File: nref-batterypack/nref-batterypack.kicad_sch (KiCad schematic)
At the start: 65 parts, among them J1 BACK_CONN, J2 C4+, J3 C3-, J4 C2+, J5 C1-, J6 C1-, J7 PACK_CONN, Q1 BC817, Q2 BC817, Q3 BC817, Q4 BC817, Q5 AO3401A, Q6 DMT2005UDV, Q7 AO3401A, SW1 Reset, U1 BQ76922

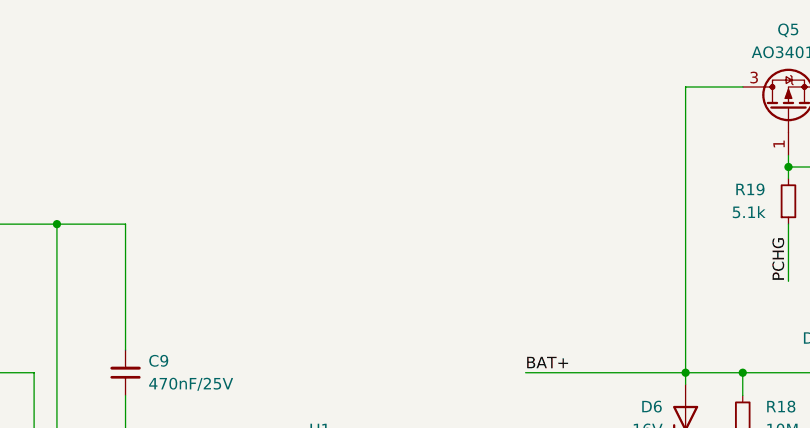
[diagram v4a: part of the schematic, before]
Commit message: batterypack front/back: update board outline/mounting holes
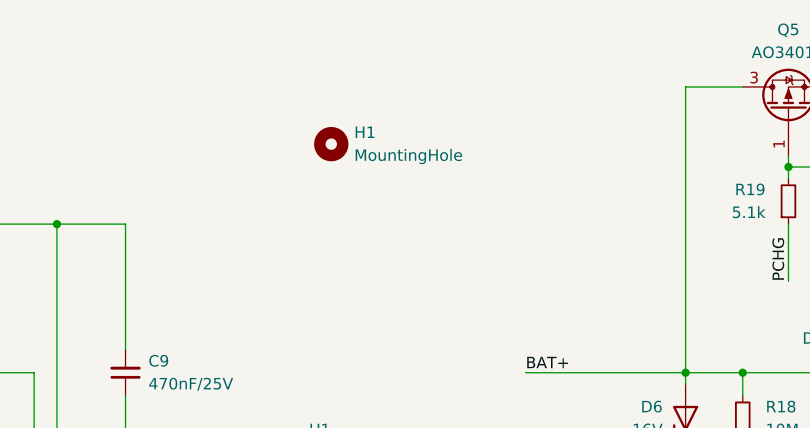
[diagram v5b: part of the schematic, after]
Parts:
- added H1: MountingHole, MountingHole:MountingHole_2.2mm_M2, symbol Mechanical:MountingHole
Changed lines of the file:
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@@
+	)
+	(symbol
+		(lib_id "Mechanical:MountingHole")
+		(at 151.13 38.1 0)
+		(unit 1)
+		(exclude_from_sim yes)
+		(in_bom no)
+		(on_board yes)
+		(dnp no)
+		(fields_autoplaced yes)
+		(property "Reference" "H1"
+			(at 153.67 36.8299 0)
+			(effects
+				(font
+					(size 1.27 1.27)
+				)
+				(justify left)
+			)
+		)
+		(property "Value" "MountingHole"
+			(at 153.67 39.3699 0)
+			(effects
+				(font
+					(size 1.27 1.27)
+				)
+				(justify left)
+			)
+		)
+		(property "Footprint" "MountingHole:MountingHole_2.2mm_M2"
+			(at 151.13 38.1 0)
+			(effects
+				(font
+					(size 1.27 1.27)
+				)
+				(hide yes)
+			)
+		)
+		(property "Datasheet" "~"
+			(at 151.13 38.1 0)
+			(effects
+				(font
+					(size 1.27 1.27)
+				)
+				(hide yes)
+			)
+		)
+		(property "Description" "Mounting Hole without connection"
+			(at 151.13 38.1 0)
+			(effects
+				(font
+					(size 1.27 1.27)
+				)
+				(hide yes)
+			)
+		)
+		(instances
+			(project ""
+				(path "/49c88381-2fae-4c42-af1a-831661a524e4"
+					(reference "H1")
+					(unit 1)
+				)
+			)
+		)
 	)
 	(symbol

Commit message: add latest PCB updates
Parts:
- H1: MPN (none) -> DNP; Manufacturer (none) -> DNP; now not fitted
- J1: footprint Connector_JST:JST_SHL_SM02B-SHLS-TF_1x02-1MP_P1.00mm_Horizontal -> Connector_JST:JST_SH_SM02B-SRSS-TB_1x02-1MP_P1.00mm_Horizontal
- J2, J3, J4, J5: MPN S7131-45R -> S1741-46R
- J7: footprint Connector_JST:JST_SHL_SM07B-SHLS-TF_1x07-1MP_P1.00mm_Horizontal -> Connector_JST:JST_SH_SM07B-SRSS-TB_1x07-1MP_P1.00mm_Horizontal
- R26: MPN RC0402JR-071KL -> (none)
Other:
- note added: "TODO: this was the wrong part, SHL instead of SH! TODO: fix footprint in layout"
- note added: "TODO: was wrong footprint!"
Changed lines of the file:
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@@
 		)
 	)
+	(text "TODO: this was the wrong part, SHL instead of SH!\nTODO: fix footprint in layout"
+		(exclude_from_sim no)
+		(at 2.794 95.758 0)
+		(effects
+			(font
+				(size 1.27 1.27)
+			)
+		)
+	)
+	(text "TODO: this was the wrong part, SHL instead of SH!\nTODO: fix footprint in layout"
+		(exclude_from_sim no)
+		(at 236.982 115.57 0)
+		(effects
+			(font
+				(size 1.27 1.27)
+			)
+		)
+	)
+	(text "TODO: was wrong footprint!"
+		(exclude_from_sim no)
+		(at 239.268 24.13 0)
+		(effects
+			(font
+				(size 1.27 1.27)
+			)
+		)
+	)
 	(label "DSG"
 		(at 168.91 113.03 180)
@@
 			)
 		)
-		(property "MPN" "RC0402JR-071KL"
+		(property "MPN" ""
 			(at 238.76 31.75 0)
 			(effects
@@
 			)
 		)
-		(property "MPN" "S7131-45R"
+		(property "MPN" "S1741-46R"
 			(at 36.83 106.68 0)
 			(effects
@@
 			)
 		)
-		(property "Footprint" "Connector_JST:JST_SHL_SM02B-SHLS-TF_1x02-1MP_P1.00mm_Horizontal"
+		(property "Footprint" "Connector_JST:JST_SH_SM02B-SRSS-TB_1x02-1MP_P1.00mm_Horizontal"
 			(at 22.86 107.95 0)
 			(effects
@@
 			)
 		)
-		(property "MPN" "S7131-45R"
+		(property "MPN" "S1741-46R"
 			(at 36.83 146.05 0)
 			(effects
@@
 			)
 		)
-		(property "MPN" "S7131-45R"
+		(property "MPN" "S1741-46R"
 			(at 36.83 63.5 0)
 			(effects
@@
 			)
 		)
-		(property "Footprint" "Connector_JST:JST_SHL_SM07B-SHLS-TF_1x07-1MP_P1.00mm_Horizontal"
+		(property "Footprint" "Connector_JST:JST_SH_SM07B-SRSS-TB_1x07-1MP_P1.00mm_Horizontal"
 			(at 238.76 129.54 0)
 			(effects
@@
 			)
 		)
-		(property "MPN" "S7131-45R"
+		(property "MPN" "S1741-46R"
 			(at 36.83 95.25 0)
 			(effects
@@
 		(in_bom no)
 		(on_board yes)
-		(dnp no)
+		(dnp yes)
 		(fields_autoplaced yes)
 		(property "Reference" "H1"
@@
 			(at 151.13 38.1 0)
 			(effects
+				(font
+					(size 1.27 1.27)
+				)
+				(hide yes)
+			)
+		)
+		(property "MPN" "DNP"
+			(at 151.13 38.1 0)
+			(effects
+				(font
+					(size 1.27 1.27)
+				)
+				(hide yes)
+			)
+		)
+		(property "Manufacturer" "DNP"
+			(at 151.13 38.1 0)
+			(effects

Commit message: batterypack: snapshot before merge
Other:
- note added: "TODO: "however, adding a Zener diode and series resistor on each pin provides more robust ESD performance""
- note added: "TODO: needs ground attachment and/or i2c protection"
- note added: "TODO: what's the return path for i2c and alert?"
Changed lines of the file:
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@@
 (kicad_sch
-	(version 20231120)
+	(version 20250114)
 	(generator "eeschema")
-	(generator_version "8.0")
+	(generator_version "9.0")
 	(paper "A4")
+	(text "TODO: what's the return path for i2c and alert?"
+		(exclude_from_sim no)
+		(at 151.13 147.32 0)
+		(effects
+			(font
+				(size 1.27 1.27)
+			)
+		)
+	)
+	(text "TODO: this was the wrong part, SHL instead of SH!\nTODO: fix footprint in layout"
+		(exclude_from_sim no)
+		(at 2.794 95.758 0)
+		(effects
+			(font
+				(size 1.27 1.27)
+			)
+		)
+	)
+	(text "TODO: \"however, adding a Zener diode and\nseries resistor on each pin provides more robust ESD performance\""
+		(exclude_from_sim no)
+		(at 238.76 104.14 0)
+		(effects
+			(font
+				(size 1.27 1.27)
+			)
+		)
+	)
+	(text "TODO: needs ground attachment and/or i2c protection"
+		(exclude_from_sim no)
+		(at 207.01 144.78 0)
+		(effects
+			(font
+				(size 1.27 1.27)
+			)
+		)
+	)
+	(text "TODO: this was the wrong part, SHL instead of SH!\nTODO: fix footprint in layout"
+		(exclude_from_sim no)
+		(at 236.982 115.57 0)
+		(effects
+			(font
+				(size 1.27 1.27)
+			)
+		)
+	)
+	(text "TODO: was wrong footprint!"
+		(exclude_from_sim no)
+		(at 239.268 24.13 0)
+		(effects
+			(font
+				(size 1.27 1.27)
+			)
+		)
+	)
 	(junction
 		(at 69.85 121.92)
@@
 		)
 	)
-	(text "TODO: this was the wrong part, SHL instead of SH!\nTODO: fix footprint in layout"
-		(exclude_from_sim no)
-		(at 2.794 95.758 0)
-		(effects
-			(font
-				(size 1.27 1.27)
-			)
-		)
-	)
-	(text "TODO: this was the wrong part, SHL instead of SH!\nTODO: fix footprint in layout"
-		(exclude_from_sim no)
-		(at 236.982 115.57 0)
-		(effects
-			(font
-				(size 1.27 1.27)
-			)
-		)
-	)
-	(text "TODO: was wrong footprint!"
-		(exclude_from_sim no)
-		(at 239.268 24.13 0)
-		(effects
-			(font
-				(size 1.27 1.27)
-			)
-		)
-	)
 	(label "DSG"
 		(at 168.91 113.03 180)
-		(fields_autoplaced yes)
 		(effects
 			(font
@@
 	(label "SDA"
 		(at 226.06 129.54 0)
-		(fields_autoplaced yes)
 		(effects
 			(font
@@
 	(label "PACK-"
 		(at 226.06 121.92 0)
-		(fields_autoplaced yes)
 		(effects
 			(font
@@
 	(label "SRP"
 		(at 101.6 163.83 180)
-		(fields_autoplaced yes)
 		(effects
 			(font
@@
 	(label "LD"
 		(at 251.46 82.55 0)
-		(fields_autoplaced yes)
 		(effects
 			(font
@@
 	(label "CHG"
 		(at 209.55 86.36 90)
-		(fields_autoplaced yes)
 		(effects
 			(font
@@
 	(label "ALERT"
 		(at 226.06 127 0)
-		(fields_autoplaced yes)
 		(effects
 			(font
@@
 	(label "VC2"
 		(at 101.6 106.68 180)
-		(fields_autoplaced yes)
 		(effects
 			(font
@@
 	(label "PACK-"
 		(at 226.06 137.16 0)
-		(fields_autoplaced yes)
 		(effects
 			(font
@@
 	(label "PDSG"
 		(at 168.91 107.95 180)
-		(fields_autoplaced yes)
 		(effects
 			(font
@@
 	(label "SCL"
 		(at 226.06 132.08 0)
-		(fields_autoplaced yes)
 		(effects
 			(font
@@
 	(label "PACK-"
 		(at 91.44 179.07 180)
-		(fields_autoplaced yes)
 		(effects
 			(font
@@
 	(label "BAT+"
 		(at 172.72 63.5 0)
-		(fields_autoplaced yes)
 		(effects
 			(font
@@
 	(label "LD"
 		(at 170.18 77.47 180)
-		(fields_autoplaced yes)
 		(effects
 			(font
@@
 	(label "DSG"
 		(at 224.79 86.36 90)
-		(fields_autoplaced yes)
 		(effects
 			(font
@@
 	(label "~{RST}"
 		(at 186.69 100.33 180)
-		(fields_autoplaced yes)
 		(effects
 			(font
@@
 	(label "CHG"
 		(at 168.91 115.57 180)
-		(fields_autoplaced yes)
 		(effects
 			(font
@@
 	(label "SCL"
 		(at 168.91 85.09 180)
-		(fields_autoplaced yes)
 		(effects
 			(font
@@
 	(label "VC4"
 		(at 101.6 83.82 180)
-		(fields_autoplaced yes)
 		(effects
 			(font
@@
 	(label "VC1"
 		(at 101.6 129.54 180)
-		(fields_autoplaced yes)
 		(effects
 			(font
@@
 	(label "PACK+"
 		(at 276.86 63.5 180)
-		(fields_autoplaced yes)
 		(effects
 			(font
@@
 	(label "VC5"
 		(at 101.6 63.5 180)
-		(fields_autoplaced yes)
 		(effects
 			(font
@@
 	(label "PACK"
 		(at 251.46 85.09 0)
-		(fields_autoplaced yes)
 		(effects
 			(font
@@
 	(label "VC0"
 		(at 101.6 151.13 180)
-		(fields_autoplaced yes)
 		(effects
 			(font
@@
 	(label "PCHG"
 		(at 168.91 110.49 180)
-		(fields_autoplaced yes)
 		(effects
 			(font
@@
 	(label "ALERT"
 		(at 168.91 90.17 180)
-		(fields_autoplaced yes)
 		(effects
 			(font
@@
 	(label "PDSG"
 		(at 228.6 53.34 90)
-		(fields_autoplaced yes)
 		(effects
 			(font
@@
 	(label "BAT-"
 		(at 43.18 158.75 0)
-		(fields_autoplaced yes)
 		(effects
 			(font
@@
 	(label "PACK+"
 		(at 226.06 124.46 0)
-		(fields_autoplaced yes)
 		(effects
 			(font
@@
 	(label "PCHG"
 		(at 201.93 53.34 90)
-		(fields_autoplaced yes)
 		(effects
 			(font
@@
 	(label "SDA"
 		(at 168.91 87.63 180)
-		(fields_autoplaced yes)
 		(effects
 			(font
@@
 	(label "BAT+"
 		(at 43.18 63.5 0)
-		(fields_autoplaced yes)
 		(effects
 			(font
@@
 	(label "C3+"
 		(at 29.21 83.82 0)
-		(fields_autoplaced yes)
 		(effects
 			(font
@@
 	(label "PACK+"
 		(at 226.06 134.62 0)
-		(fields_autoplaced yes)
 		(effects
 			(font
@@
 	(label "PACK"
 		(at 170.18 80.01 180)
-		(fields_autoplaced yes)
 		(effects
 			(font
@@
 	(label "SRN"
 		(at 101.6 171.45 180)
-		(fields_autoplaced yes)
 		(effects
 			(font
@@
 	(label "C1+"
 		(at 29.21 129.54 0)
-		(fields_autoplaced yes)
 		(effects
 			(font
@@
 		)
 	)
+	(embedded_fonts no)
 )
